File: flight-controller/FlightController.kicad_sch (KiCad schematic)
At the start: 9 parts, among them U1 ESP32-WROOM-32E, U2 TPS629210

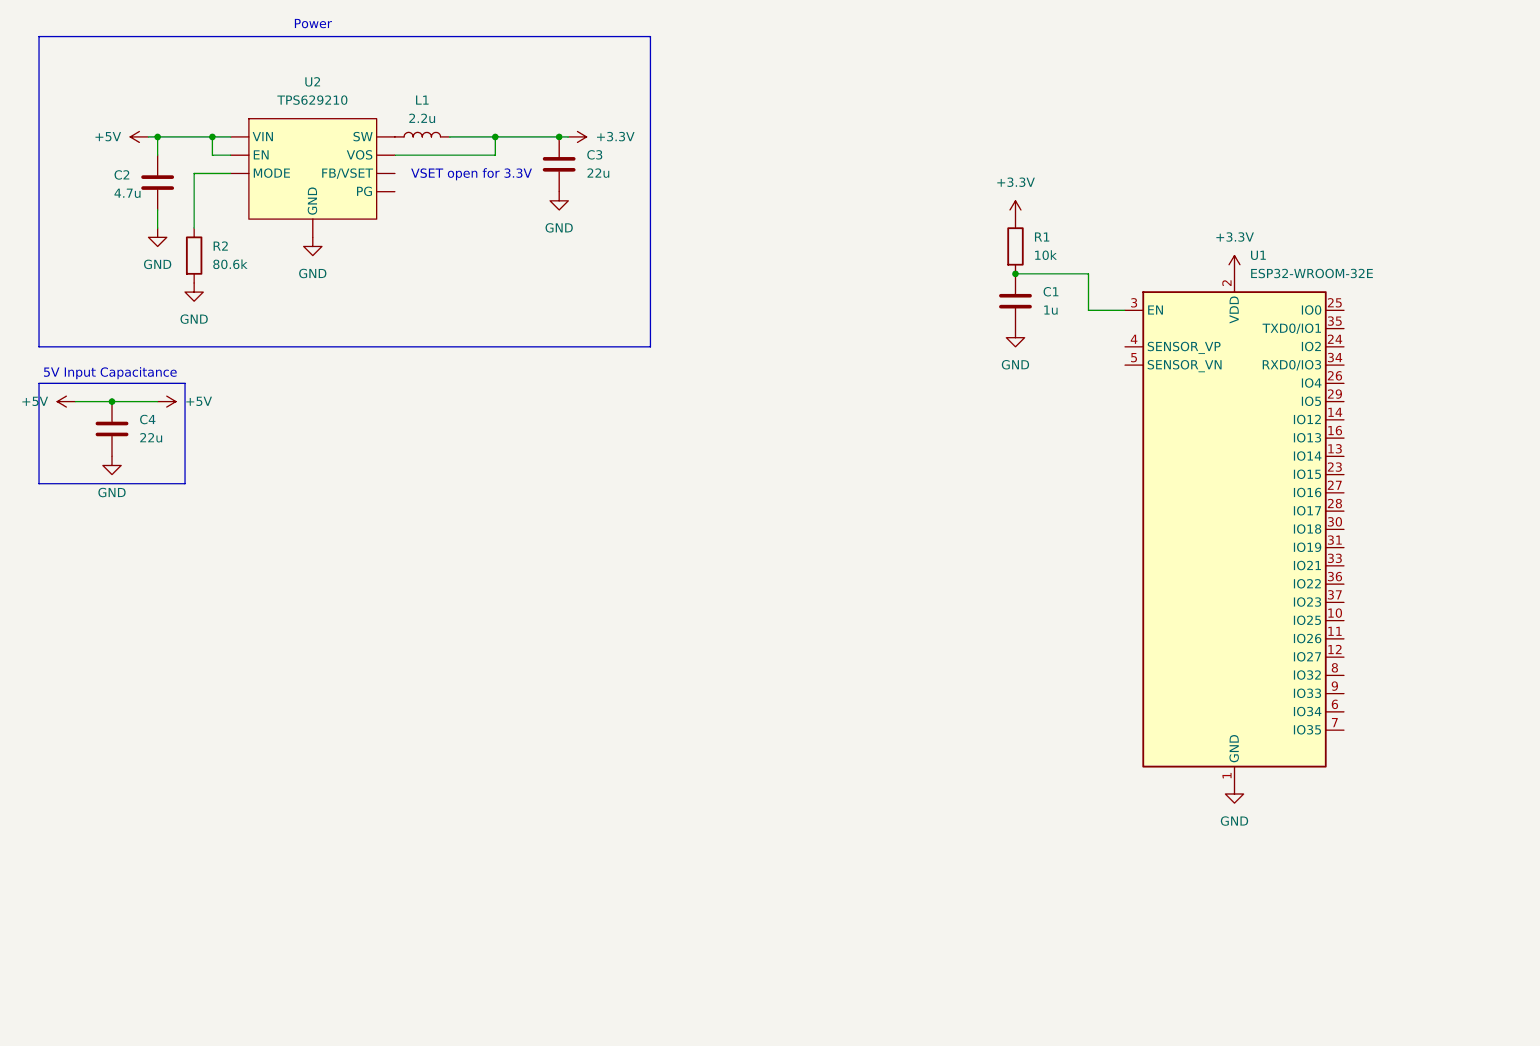
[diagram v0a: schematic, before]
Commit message: switch to new esp with native usb
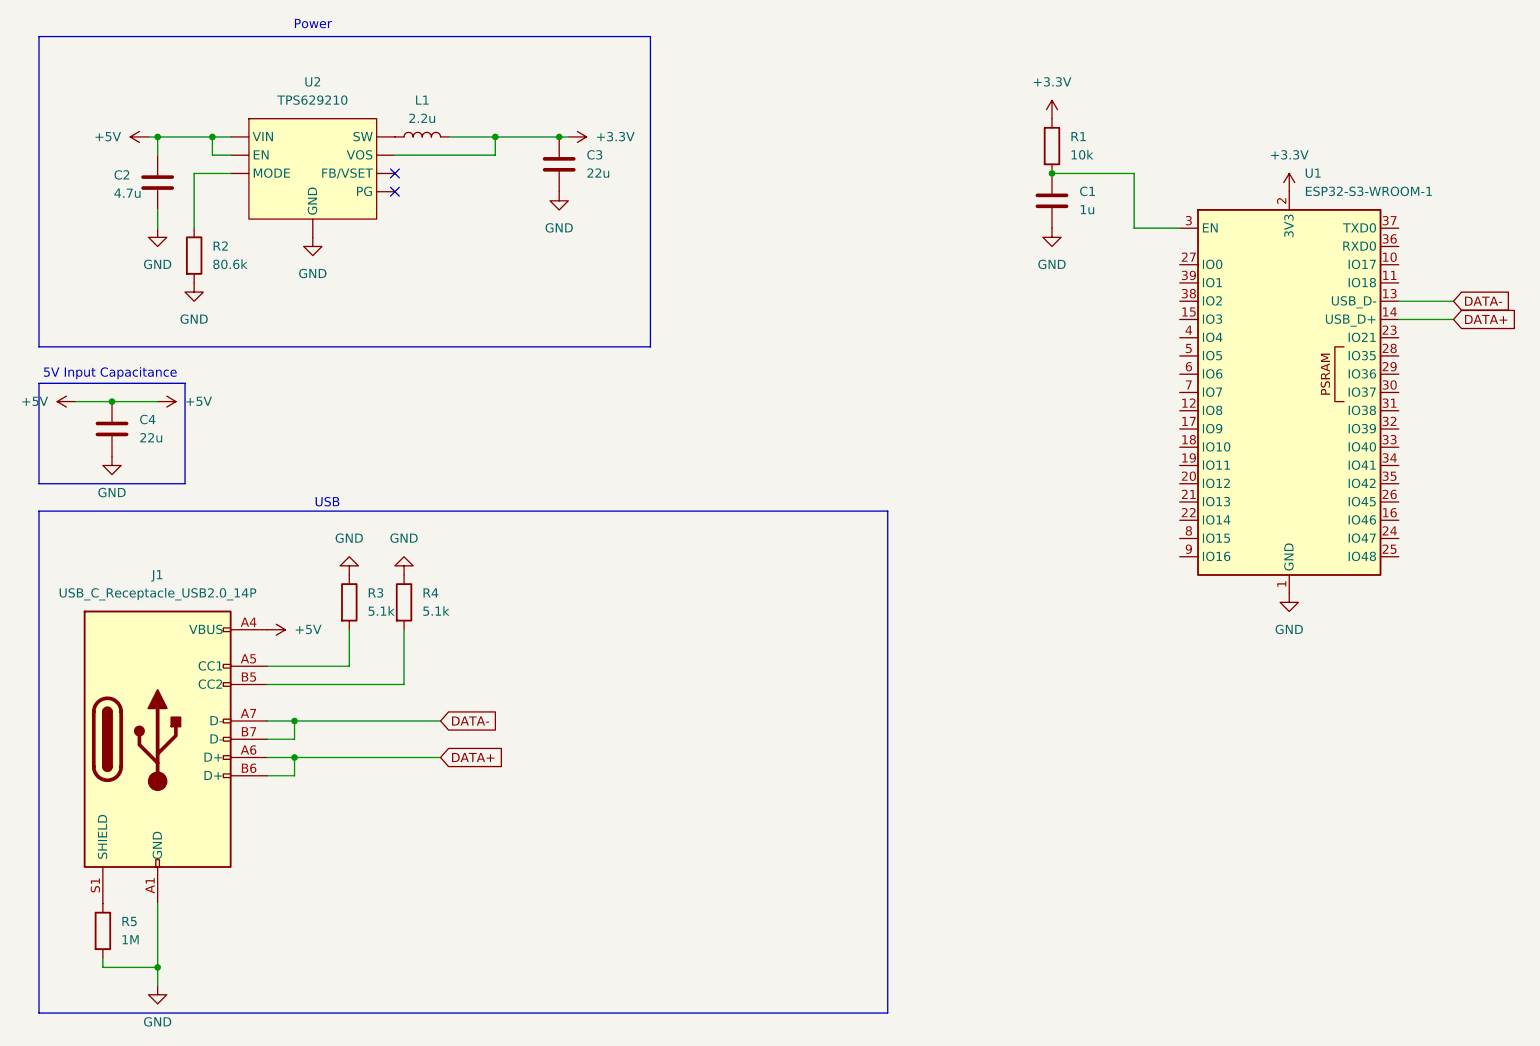
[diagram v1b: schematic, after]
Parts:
- removed U1: ESP32-WROOM-32E, RF_Module:ESP32-WROOM-32D, symbol RF_Module:ESP32-WROOM-32E
- added J1: USB_C_Receptacle_USB2.0_14P, symbol Connector:USB_C_Receptacle_USB2.0_14P
- added R3, R4: 5.1k, symbol Device:R
- added R5: 1M, symbol Device:R
- added U1: ESP32-S3-WROOM-1, RF_Module:ESP32-S3-WROOM-1, symbol RF_Module:ESP32-S3-WROOM-1
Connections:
- net +3.3V: now also U1.2 (3V3)
- net +5V: now also J1.A4 (VBUS), J1.A9 (VBUS), J1.B4 (VBUS), J1.B9 (VBUS)
- net GND: now also J1.A1 (GND), J1.A12 (GND), J1.B1 (GND), J1.B12 (GND), R3.1, R4.1, R5.2, U1.1 (GND), U1.40 (GND), U1.41 (GND)
- net at C1.1, R1.2: now also U1.3 (EN)
- new net: J1.A5 (CC1), R3.2
- new net: J1.B5 (CC2), R4.2
- new net: J1.S1 (SHIELD), R5.1
- new net DATA+: J1.A6 (D+), J1.B6 (D+), U1.14 (USB_D+)
- new net DATA-: J1.A7 (D-), J1.B7 (D-), U1.13 (USB_D-)
- no-connect marks 0 -> 2
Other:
- note added: "USB"
- note removed: "VSET open for 3.3V"

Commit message: Add a bunch of sensors
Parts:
- added C10, C5, C6, C9: 100n, symbol Device:C
- added C7: 1u, symbol Device:C
- added C8: 10u, symbol Device:C
- added J2, J3, J4, J5: Conn_01x03_Pin, symbol Connector:Conn_01x03_Pin
- added U3: MMC5983MA, MMC5983MA:PQFN50P300X300X100-16N, symbol MMC5983MA:MMC5983MA
- added U4: BMI270, BMI270:XDCR_BMI270, symbol BMI270:BMI270
- added U5: BMP581, BMP581:BMP581, symbol BMP581:BMP581
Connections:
- net +3.3V: now also C10.2, C5.2, C6.1, C7.2, C9.2, U3.13 (VDDIO), U3.2 (VDD), U3.4 (~{SPI_CS}), U4.5 (VDDIO), U4.8 (VDD), U5.1 (VDDIO), U5.10 (VDD), U5.6 (CSB)
- net +5V: now also J2.2 (Pin_2), J3.2 (Pin_2), J4.2 (Pin_2), J5.2 (Pin_2)
- net GND: now also C10.1, C5.1, C6.2, C7.1, C8.2, C9.1, J2.3 (Pin_3), J3.3 (Pin_3), J4.3 (Pin_3), J5.3 (Pin_3), U3.11 (GND), U3.9 (GND), U4.6 (GNDIO), U4.7 (GND), U5.3 (VSS_1), U5.8 (VSS_2), U5.9 (VSS_3)
- new net: C8.1, U3.10 (CAP)
- new net: U3.12 (NC), U3.14 (NC), U3.3 (NC), U3.6 (NC), U3.7 (NC), U3.8 (NC)
- new net I2C_INT: U5.7 (INT)
- new net I2C_SCL: U3.1 (SCL/SPI_SCK), U5.2 (SCK)
- new net I2C_SDA: U3.16 (SDA/SPI_SDI), U5.4 (SDI)
- new net IMU_CS: U4.12 (CSB)
- new net IMU_INT: U4.4 (INT1)
- new net IMU_SCL: U4.13 (SCX)
- new net IMU_SDA: U4.14 (SDX)
- new net IMU_SDO: U4.1 (SDO)
- new net MAG_INT: U3.15 (INT)
- new net MOTOR1_PWM: J2.1 (Pin_1)
- new net MOTOR2_PWM: J3.1 (Pin_1)
- new net MOTOR3_PWM: J4.1 (Pin_1)
- new net MOTOR4_PWM: J5.1 (Pin_1)
- no-connect marks 2 -> 10
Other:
- note added: "Barometer"
- note added: "ESC Plugs"
- note added: "IMU"
- note added: "Magnetometer"
- moved on the sheet: C1, R1, U1

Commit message: schematic should be done
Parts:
- removed U2: TPS629210, symbol FC_parts:TPS629210
- added J7: Micro_SD_Card_Det1, symbol Connector:Micro_SD_Card_Det1
- added J8: Conn_01x06_Pin, symbol Connector:Conn_01x06_Pin
- added R6, R7: 2.7k, symbol Device:R
- added U2: TPS629210DRLR, TPS629210DRLR:SOT50P160X60-8N, symbol TPS629210DRLR:TPS629210DRLR
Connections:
- net I2C_INT is gone; now on net BARO_INT: U5.7 (INT)
- net +3.3V: now also U5.5 (SDO), J7.4 (VDD), R6.1, R7.1, U2.3 (VOS)
- net +5V: now also U2.6 (VIN), U2.7 (EN)
- net GND: now also J7.10 (SHIELD), J7.6 (VSS), U2.5 (GND)
- net I2C_SCL: now also U1.12 (IO8), R6.2
- net I2C_SDA: now also U1.17 (IO9), R7.2
- net IMU_CS: now also U1.18 (IO10)
- net IMU_INT: now also U1.22 (IO14)
- net IMU_SCL: now also U1.20 (IO12)
- net IMU_SDA: now also U1.19 (IO11)
- net IMU_SDO: now also U1.21 (IO13)
- net MAG_INT: now also U1.23 (IO21)
- net MOTOR1_PWM: now also U1.4 (IO4)
- net MOTOR2_PWM: now also U1.5 (IO5)
- net MOTOR3_PWM: now also U1.6 (IO6)
- net MOTOR4_PWM: now also U1.7 (IO7)
- net at R2.1: now also U2.8 (MODE/S-CONF)
- net at L1.1: now also U2.4 (SW)
- net IO17: now reaches U1.10 (IO17)
- net IO17: now also J8.5 (Pin_5)
- net IO18: now reaches U1.11 (IO18)
- net IO18: now also J8.6 (Pin_6)
- net BARO_INT: now reaches U1.24 (IO47)
- net SD_CD: now reaches U1.31 (IO38)
- net SD_CD: now also J7.9 (DET)
- net SD_CLK: now reaches U1.32 (IO39)
- net SD_CLK: now also J7.5 (CLK)
- net SD_MOSI: now reaches U1.33 (IO40)
- net SD_MOSI: now also J7.3 (CMD)
- net SD_MISO: now reaches U1.34 (IO41)
- net SD_MISO: now also J7.7 (DAT0)
- net SD_CS: now reaches U1.35 (IO42)
- net SD_CS: now also J7.2 (DAT3/CD)
- net IO2: now reaches U1.38 (IO2)
- net IO2: now also J8.2 (Pin_2)
- net IO1: now reaches U1.39 (IO1)
- net IO1: now also J8.1 (Pin_1)
- net IO15: now reaches U1.8 (IO15)
- net IO15: now also J8.3 (Pin_3)
- net IO16: now reaches U1.9 (IO16)
- net IO16: now also J8.4 (Pin_4)
- no-connect marks 10 -> 21
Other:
- note added: "Pins"
- note removed: "ESC Plugs"
- moved on the sheet: C2, C3, L1, R2

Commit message: update usb
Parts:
- removed J1: USB_C_Receptacle_USB2.0_14P, symbol Connector:USB_C_Receptacle_USB2.0_14P
- removed R5: 1M, symbol Device:R
- added J6: USB4215-03-A_REVA, USB4215-03-A_REVA:GCT_USB4215-03-A_REVA, symbol USB4215-03-A_REVA:USB4215-03-A_REVA
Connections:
- net +5V: now also J6.A4_B9 (VBUS_A), J6.B4_A9 (VBUS_B)
- net DATA+: now also J6.A6 (DP1), J6.B6 (DP2)
- net DATA-: now also J6.A7 (DN1), J6.B7 (DN2)
- net GND: now also J6.A1_B12 (GND_A), J6.B1_A12 (GND_B), J6.SH1 (SHIELD), J6.SH2 (SHIELD__1), J6.SH3 (SHIELD__2), J6.SH4 (SHIELD__3)
- net at R3.2: now also J6.B5 (CC2)
- net at R4.2: now also J6.A5 (CC1)
- no-connect marks 21 -> 23
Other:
- moved on the sheet: R4

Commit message: add footprints
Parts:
- removed J7: Micro_SD_Card_Det1, symbol Connector:Micro_SD_Card_Det1
- added J1: MSD-4-A, MSD-4-A:CUI_MSD-4-A, symbol MSD-4-A:MSD-4-A
- C1, C10, C2, C3, C4, C5, C6, C7, C8, C9: footprint (none) -> Capacitor_SMD:C_0603_1608Metric_Pad1.08x0.95mm_HandSolder
- J2, J3, J4, J5: footprint (none) -> Connector_PinHeader_2.54mm:PinHeader_1x03_P2.54mm_Vertical
- J8: footprint (none) -> Connector_PinHeader_2.54mm:PinHeader_1x06_P2.54mm_Vertical
- L1: footprint (none) -> Inductor_SMD:L_1008_2520Metric_Pad1.43x2.20mm_HandSolder
- R1, R2, R3, R4, R6, R7: footprint (none) -> Resistor_SMD:R_0603_1608Metric_Pad0.98x0.95mm_HandSolder
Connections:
- net +3.3V: now also J1.4 (VDD)
- net GND: now also J1.6 (VSS), J1.G1 (COVER_GND), J1.G2 (COVER_GND__1), J1.G3 (COVER_GND__2), J1.G4 (COVER_GND__3)
- net SD_CD: now also J1.CD
- net SD_CLK: now also J1.5 (CLK)
- net SD_CS: now also J1.2 (CD/DAT3)
- net SD_MISO: now also J1.7 (DAT0)
- net SD_MOSI: now also J1.3 (CMD)
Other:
- note added: "SD Card"

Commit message: general component locations
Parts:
- removed J8: Conn_01x06_Pin, Connector_PinHeader_2.54mm:PinHeader_1x06_P2.54mm_Vertical, symbol Connector:Conn_01x06_Pin
- added J7, J8: Conn_01x03_Pin, Connector_PinHeader_2.54mm:PinHeader_1x03_P2.54mm_Vertical, symbol Connector:Conn_01x03_Pin
- J1: footprint MSD-4-A:CUI_MSD-4-A -> MSD_4_A:CUI_MSD-4-A
- J6: footprint USB4215-03-A_REVA:GCT_USB4215-03-A_REVA -> USB4215_03_A:GCT_USB4215-03-A_REVA
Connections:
- net IO1 is gone; now on net MOTOR3_PWM: U1.39 (IO1)
- net IO15 is gone; now on net SD_CLK: U1.8 (IO15)
- net IO16 is gone; now on net SD_MOSI: U1.9 (IO16)
- net IO17 is gone; now on net SD_CS: U1.10 (IO17)
- net IO2 is gone; now on net MOTOR4_PWM: U1.38 (IO2)
- net +5V: now also J7.2 (Pin_2)
- net GND: now also J7.3 (Pin_3)
- net I2C_SCL: now also U1.31 (IO38); no longer U1.12 (IO8)
- net I2C_SDA: now also U1.32 (IO39); no longer U1.17 (IO9)
- net IMU_CS: now also U1.22 (IO14); no longer U1.18 (IO10)
- net IMU_INT: now also U1.18 (IO10); no longer U1.22 (IO14)
- net IMU_SCL: now also U1.21 (IO13); no longer U1.20 (IO12)
- net IMU_SDA: now also U1.20 (IO12); no longer U1.19 (IO11)
- net IMU_SDO: now also U1.19 (IO11); no longer U1.21 (IO13)
- net MOTOR3_PWM: no longer U1.6 (IO6)
- net MOTOR4_PWM: no longer U1.7 (IO7)
- net SD_CD: now also U1.6 (IO6); no longer U1.31 (IO38)
- net SD_CLK: no longer U1.32 (IO39)
- net SD_CS: no longer U1.35 (IO42)
- net SD_MISO: now also U1.7 (IO7); no longer U1.34 (IO41)
- net SD_MOSI: no longer U1.33 (IO40)
- net IO18 renamed RECEIVER
- net RECEIVER: now also J7.1 (Pin_1)
- new net IO40: J8.1 (Pin_1), U1.33 (IO40)
- new net IO41: J8.2 (Pin_2), U1.34 (IO41)
- new net IO42: J8.3 (Pin_3), U1.35 (IO42)
- new net IO8: U1.12 (IO8)
- new net IO9: U1.17 (IO9)

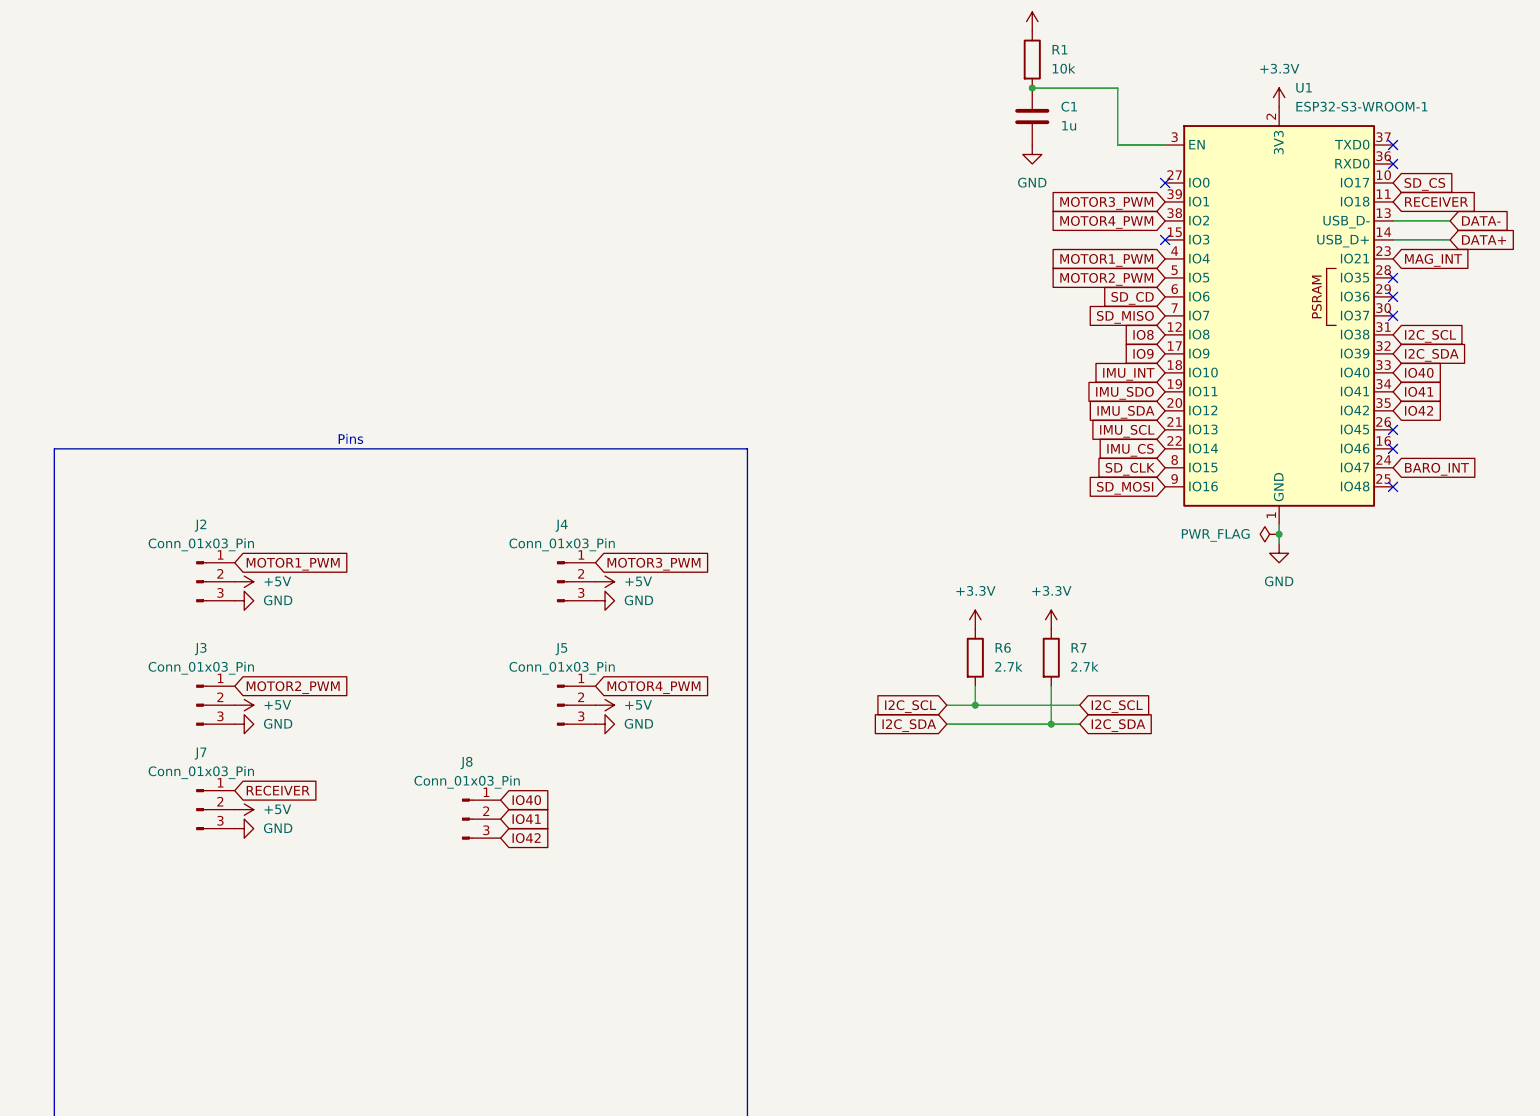
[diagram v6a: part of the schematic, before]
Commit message: add uart header
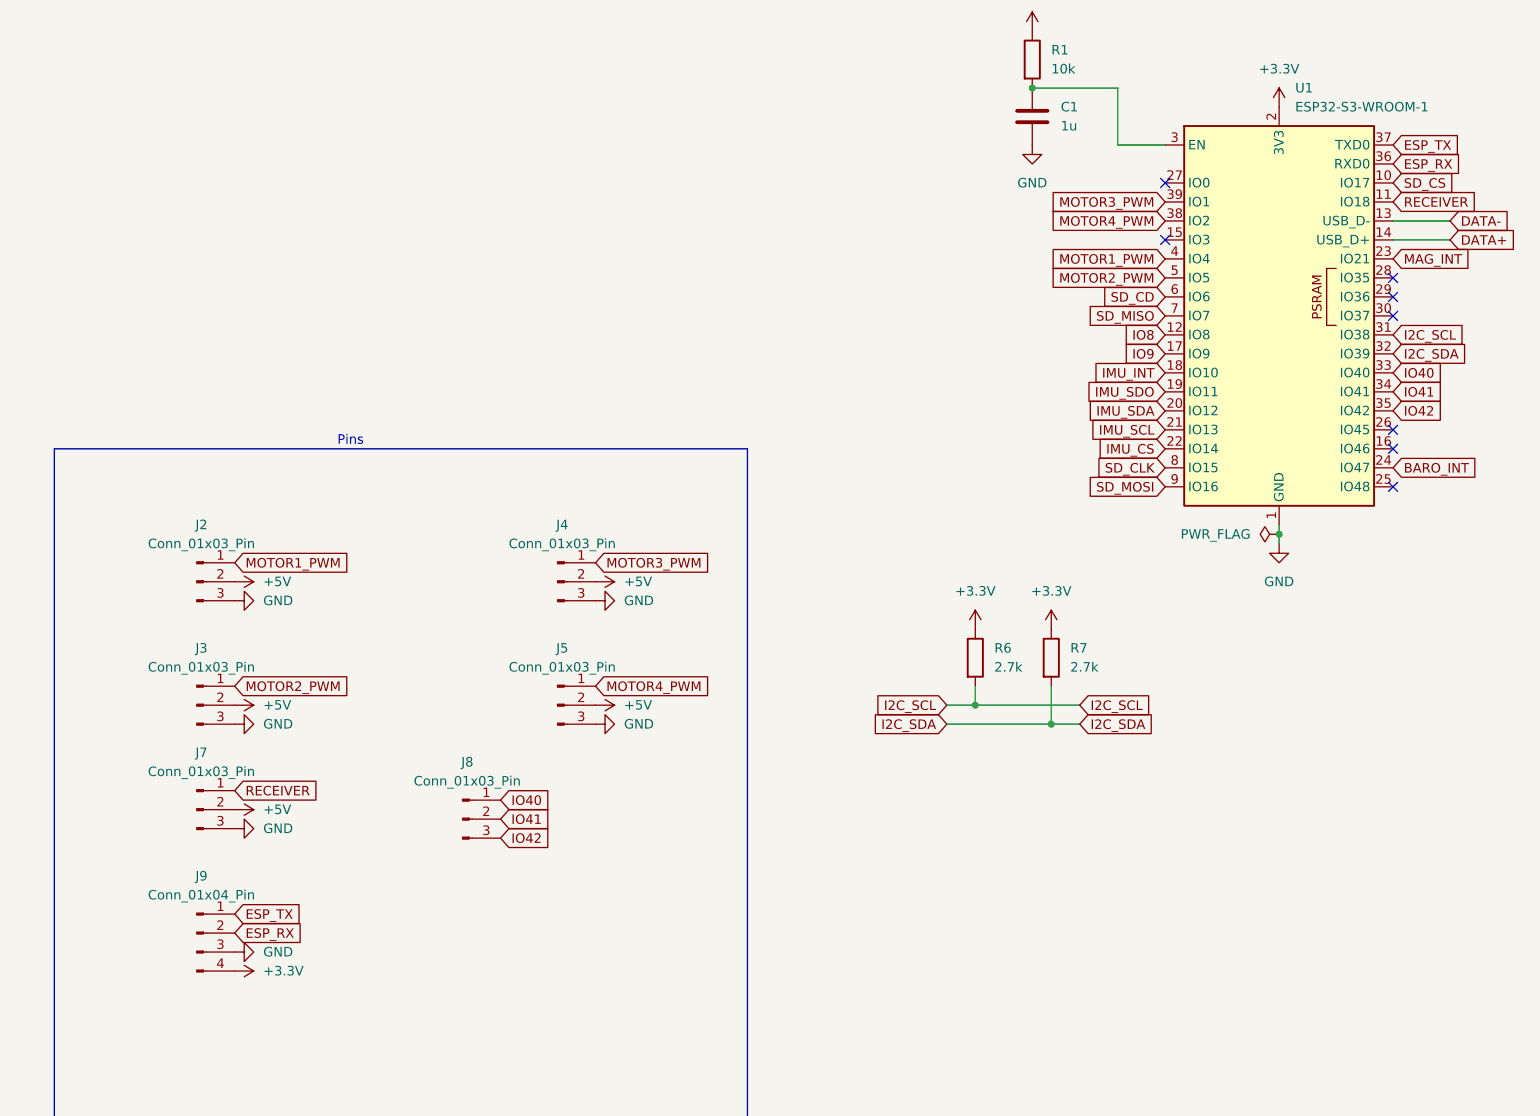
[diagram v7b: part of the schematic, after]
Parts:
- added J9: Conn_01x04_Pin, Connector_PinHeader_2.54mm:PinHeader_1x04_P2.54mm_Vertical, symbol Connector:Conn_01x04_Pin
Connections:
- net +3.3V: now also J9.4 (Pin_4)
- net GND: now also J9.3 (Pin_3)
- net ESP_RX: now reaches U1.36 (RXD0)
- net ESP_RX: now also J9.2 (Pin_2)
- net ESP_TX: now reaches U1.37 (TXD0)
- net ESP_TX: now also J9.1 (Pin_1)
- no-connect marks 23 -> 21
